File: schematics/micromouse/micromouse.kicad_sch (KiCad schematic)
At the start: 63 parts, among them J1 TOF_LEFT, J10 MotorB_Conn, J11 BMI_ConnB, J12 BMI_ConnA, J13 StepDown_{In+}, J14 StepDown_{In-}, J15 StepDown_{Out+}, J16 StepDown_{Out-}, J2 TOF_FRONTLEFT, J3 TOF_FRONTRIGHT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

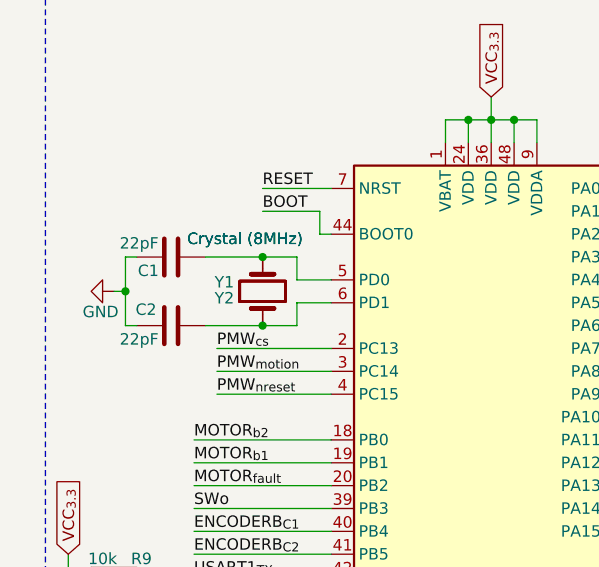
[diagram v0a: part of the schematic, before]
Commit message: Schematic/PCB: Add missing resistor for Crystal, based on STM's AN2586 (Getting started with STM32F10xxx hardware development).
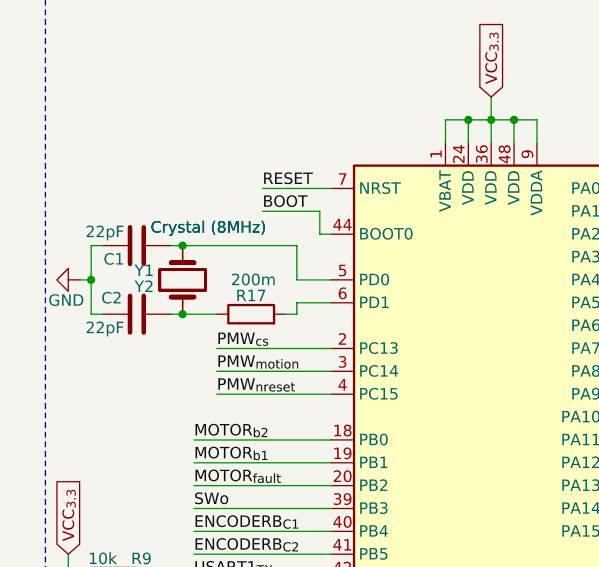
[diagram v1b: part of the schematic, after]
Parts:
- added R17: 200m, Resistor_SMD:R_0805_2012Metric_Pad1.20x1.40mm_HandSolder, symbol Device:R
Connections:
- net at C2.1, Y1.1, Y2.1: now also R17.1; no longer U1.6 (PD1)
- new net: R17.2, U1.6 (PD1)
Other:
- moved on the sheet: C1, C2, Y1, Y2
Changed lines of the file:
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@@
 	)
 	(junction
+		(at 27.94 43.18)
+		(diameter 0)
+		(color 0 0 0 0)
+	)
+	(junction
 		(at 60.96 111.76)
 		(diameter 0)
@@
 	)
 	(junction
-		(at 36.83 44.45)
-		(diameter 0)
-		(color 0 0 0 0)
-	)
-	(junction
 		(at 193.04 120.65)
 		(diameter 0)
@@
 	)
 	(junction
-		(at 36.83 52.07)
-		(diameter 0)
-		(color 0 0 0 0)
-	)
-	(junction
 		(at 123.19 135.89)
 		(diameter 0)
@@
 	)
 	(junction
-		(at 21.59 48.26)
+		(at 17.78 46.99)
 		(diameter 0)
 		(color 0 0 0 0)
@@
 	)
 	(junction
+		(at 27.94 50.8)
+		(diameter 0)
+		(color 0 0 0 0)
+	)
+	(junction
 		(at 255.27 123.19)
 		(diameter 0)
@@
 	(wire
 		(pts
-			(xy 30.48 52.07) (xy 36.83 52.07)
+			(xy 26.67 50.8) (xy 27.94 50.8)
 		)
 		(stroke
@@
 	(wire
 		(pts
-			(xy 40.64 52.07) (xy 36.83 52.07)
-		)
-		(stroke
-			(width 0)
-			(type default)
-		)
-	)
-	(wire
-		(pts
 			(xy 167.64 74.93) (xy 167.64 92.71)
 		)
@@
 	(wire
 		(pts
-			(xy 40.64 44.45) (xy 40.64 46.99)
+			(xy 40.64 43.18) (xy 40.64 46.99)
 		)
 		(stroke
@@
 	(wire
 		(pts
-			(xy 22.86 44.45) (xy 21.59 44.45)
+			(xy 19.05 43.18) (xy 17.78 43.18)
 		)
 		(stroke
@@
 	(wire
 		(pts
-			(xy 21.59 44.45) (xy 21.59 48.26)
+			(xy 17.78 43.18) (xy 17.78 46.99)
 		)
 		(stroke
@@
 	(wire
 		(pts
-			(xy 20.32 48.26) (xy 21.59 48.26)
+			(xy 16.51 46.99) (xy 17.78 46.99)
 		)
 		(stroke
@@
 	(wire
 		(pts
-			(xy 21.59 48.26) (xy 21.59 52.07)
+			(xy 17.78 46.99) (xy 17.78 50.8)
 		)
 		(stroke
@@
 	(wire
 		(pts
+			(xy 27.94 50.8) (xy 31.75 50.8)
+		)
+		(stroke
+			(width 0)
+			(type default)
+		)
+	)
+	(wire
+		(pts
 			(xy 130.81 187.96) (xy 138.43 187.96)
 		)
@@
 	(wire
 		(pts
+			(xy 27.94 43.18) (xy 40.64 43.18)
+		)
+		(stroke
+			(width 0)
+			(type default)
+		)
+	)
+	(wire
+		(pts
 			(xy 172.72 76.2) (xy 172.72 92.71)
 		)
@@
 	(wire
 		(pts
-			(xy 21.59 52.07) (xy 22.86 52.07)
+			(xy 17.78 50.8) (xy 19.05 50.8)
 		)
 		(stroke
@@
 	(wire
 		(pts
-			(xy 40.64 49.53) (xy 40.64 52.07)
-		)
-		(stroke
-			(width 0)
-			(type default)
-		)
-	)
-	(wire
-		(pts
-			(xy 36.83 44.45) (xy 40.64 44.45)
+			(xy 40.64 49.53) (xy 40.64 50.8)
 		)
 		(stroke
@@
 	(wire
 		(pts
-			(xy 30.48 44.45) (xy 36.83 44.45)
+			(xy 26.67 43.18) (xy 27.94 43.18)
 		)
 		(stroke
@@
 		)
 	)
+	(wire
+		(pts
+			(xy 39.37 50.8) (xy 40.64 50.8)
+		)
+		(stroke
+			(width 0)
+			(type default)
+		)
+	)
 	(rectangle
 		(start 12.7 12.7)
@@
 	(symbol
 		(lib_id "power:GND")
-		(at 20.32 48.26 270)
+		(at 16.51 46.99 270)
 		(unit 1)
 		(exclude_from_sim no)
@@
 		(dnp no)
 		(property "Reference" "#PWR014"
-			(at 13.97 48.26 0)
+			(at 10.16 46.99 0)
 			(effects
 				(font
@@
 		)
 		(property "Value" "GND"
-			(at 20.828 50.546 90)
+			(at 17.018 49.276 90)
 			(effects
 				(font
@@
 		)
 		(property "Footprint" ""
-			(at 20.32 48.26 0)
+			(at 16.51 46.99 0)
 			(effects
 				(font
@@
 		)
 		(property "Datasheet" ""
-			(at 20.32 48.26 0)
+			(at 16.51 46.99 0)
 			(effects
 				(font
@@
 		)
 		(property "Description" "Power symbol creates a global label with name \"GND\" , ground"
-			(at 20.32 48.26 0)
+			(at 16.51 46.99 0)
 			(effects
 				(font
@@
 	(symbol
 		(lib_id "Device:C")
-		(at 26.67 52.07 270)
+		(at 22.86 50.8 270)
 		(unit 1)
 		(exclude_from_sim no)
@@
 		(dnp no)
 		(property "Reference" "C2"
-			(at 23.876 50.292 90)
+			(at 20.066 49.022 90)
 			(effects
 				(font
@@
 		)
 		(property "Value" "22pF"
-			(at 23.114 53.594 90)
+			(at 19.304 52.324 90)
 			(effects
 				(font
@@
 		)
 		(property "Footprint" "Capacitor_SMD:C_0805_2012Metric_Pad1.18x1.45mm_HandSolder"
-			(at 22.86 53.0352 0)
+			(at 19.05 51.7652 0)
 			(effects
 				(font
@@
 		)
 		(property "Datasheet" "~"
-			(at 26.67 52.07 0)
+			(at 22.86 50.8 0)
 			(effects
 				(font
@@
 		)
 		(property "Description" "Unpolarized capacitor"
-			(at 26.67 52.07 0)
+			(at 22.86 50.8 0)
 			(effects
 				(font
@@
 	(symbol
 		(lib_id "Device:C")
-		(at 26.67 44.45 90)
+		(at 22.86 43.18 90)
 		(unit 1)
 		(exclude_from_sim no)
@@
 		(dnp no)
 		(property "Reference" "C1"
-			(at 24.13 45.974 90)
+			(at 20.32 44.704 90)
 			(effects
 				(font
@@
 		)
 		(property "Value" "22pF"
-			(at 23.114 42.926 90)
+			(at 19.304 41.656 90)
 			(effects
 				(font
@@
 		)
 		(property "Footprint" "Capacitor_SMD:C_0805_2012Metric_Pad1.18x1.45mm_HandSolder"
-			(at 30.48 43.4848 0)
+			(at 26.67 42.2148 0)
 			(effects
 				(font
@@
 		)
 		(property "Datasheet" "~"
-			(at 26.67 44.45 0)
+			(at 22.86 43.18 0)
 			(effects
 				(font
@@
 		)
 		(property "Description" "Unpolarized capacitor"
-			(at 26.67 44.45 0)
+			(at 22.86 43.18 0)
 			(effects
 				(font
@@
 	(symbol
 		(lib_id "Device:Crystal")
-		(at 36.83 48.26 90)
+		(at 27.94 46.99 90)
 		(unit 1)
 		(exclude_from_sim no)
@@
 		(dnp no)
 		(property "Reference" "Y1"
-			(at 31.496 47.244 90)
+			(at 22.606 45.974 90)
 			(effects
 				(font
@@
 		)
 		(property "Value" "Crystal (8MHz)"
-			(at 28.448 42.418 90)
+			(at 24.384 41.148 90)
 			(effects
 				(font
@@
 		)
 		(property "Footprint" "Crystal:Crystal_SMD_HC49-SD"
-			(at 36.83 48.26 0)
+			(at 27.94 46.99 0)
 			(effects
 				(font
@@
 		)
 		(property "Datasheet" "~"
-			(at 36.83 48.26 0)
+			(at 27.94 46.99 0)
 			(effects
 				(font
@@
 		)
 		(property "Description" "Two pin crystal"
-			(at 36.83 48.26 0)
+			(at 27.94 46.99 0)
 			(effects
 				(font
@@
 	(symbol
 		(lib_id "Device:Crystal")
-		(at 36.83 48.26 90)
+		(at 27.94 46.99 90)
 		(unit 1)
 		(exclude_from_sim no)
@@
 		(dnp no)
 		(property "Reference" "Y2"
-			(at 31.496 49.022 90)
+			(at 22.606 47.752 90)
 			(effects
 				(font
@@
 		)
 		(property "Value" "Crystal (8MHz)"
-			(at 28.448 42.418 90)
+			(at 24.384 41.148 90)
 			(effects
 				(font
@@
 		)
 		(property "Footprint" "Crystal:Crystal_HC49-4H_Vertical"
-			(at 36.83 48.26 0)
+			(at 27.94 46.99 0)
 			(effects
 				(font
@@
 		)
 		(property "Datasheet" "~"
-			(at 36.83 48.26 0)
+			(at 27.94 46.99 0)
 			(effects
 				(font
@@
 		)
 		(property "Description" "Two pin crystal"
-			(at 36.83 48.26 0)
+			(at 27.94 46.99 0)
 			(effects
 				(font
@@
 					(unit 1)
 				)
+			)
+		)
+	)
+	(symbol
+		(lib_id "Device:R")
+		(at 35.56 50.8 90)
+		(unit 1)
+		(exclude_from_sim no)
+		(in_bom yes)
+		(on_board yes)
+		(dnp no)
+		(property "Reference" "R17"
+			(at 35.56 48.768 90)
+			(effects
+				(font
+					(size 1.27 1.27)
+				)
+			)
+		)
+		(property "Value" "200m"
+			(at 35.814 46.99 90)
+			(effects
+				(font
+					(size 1.27 1.27)
+				)
+			)
+		)
+		(property "Footprint" "Resistor_SMD:R_0805_2012Metric_Pad1.20x1.40mm_HandSolder"
+			(at 35.56 52.578 90)
+			(effects
+				(font
+					(size 1.27 1.27)
+				)
+				(hide yes)
+			)
+		)
+		(property "Datasheet" "~"
+			(at 35.56 50.8 0)
+			(effects
+				(font
+					(size 1.27 1.27)
+				)
+				(hide yes)
+			)
+		)
+		(property "Description" "Resistor"
+			(at 35.56 50.8 0)
+			(effects
+				(font
+					(size 1.27 1.27)
+				)
+				(hide yes)
+			)
+		)
+		(pin "2"
+		)
+		(pin "1"
+		)
+		(instances
+			(project "micromouse"
+				(path "/48923552-97ee-4377-b66c-70fa2ca23716"
+					(reference "R17")
+					(unit 1)
+				)

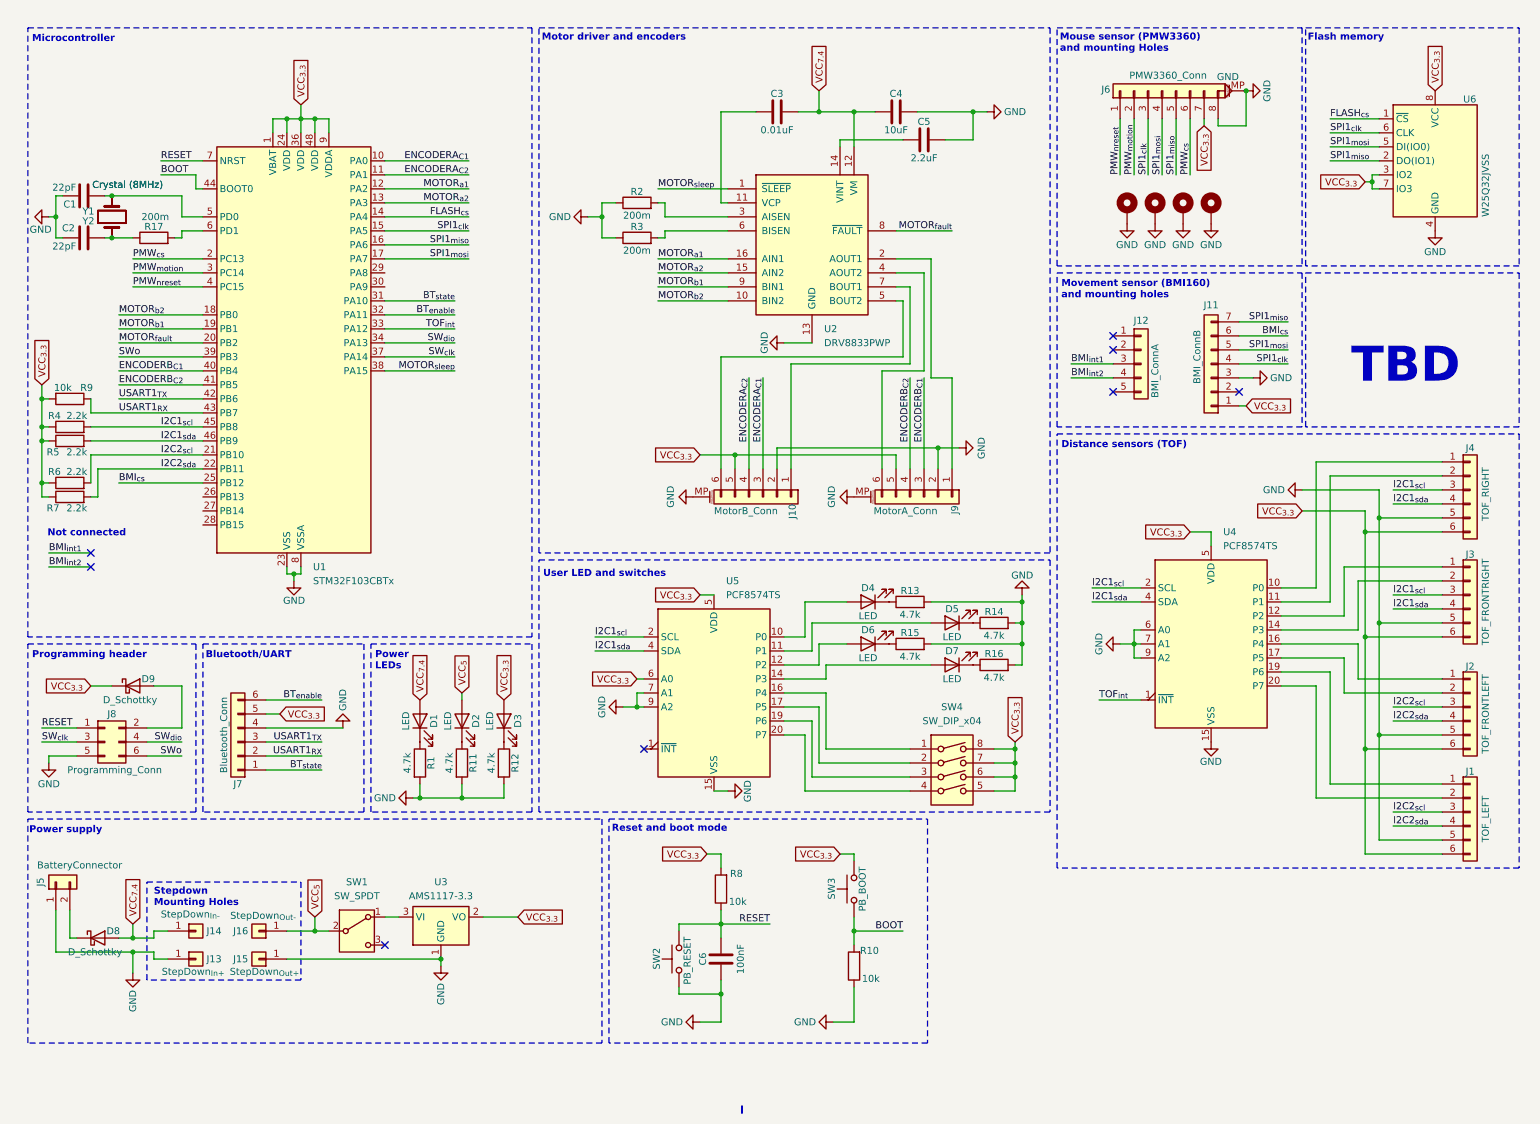
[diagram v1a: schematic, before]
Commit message: Schematic: * Add microSD card socket
PCB:
* Change BOOT and RESET buttons
* Add and connect microSD card socket
* Fix some CRC errors
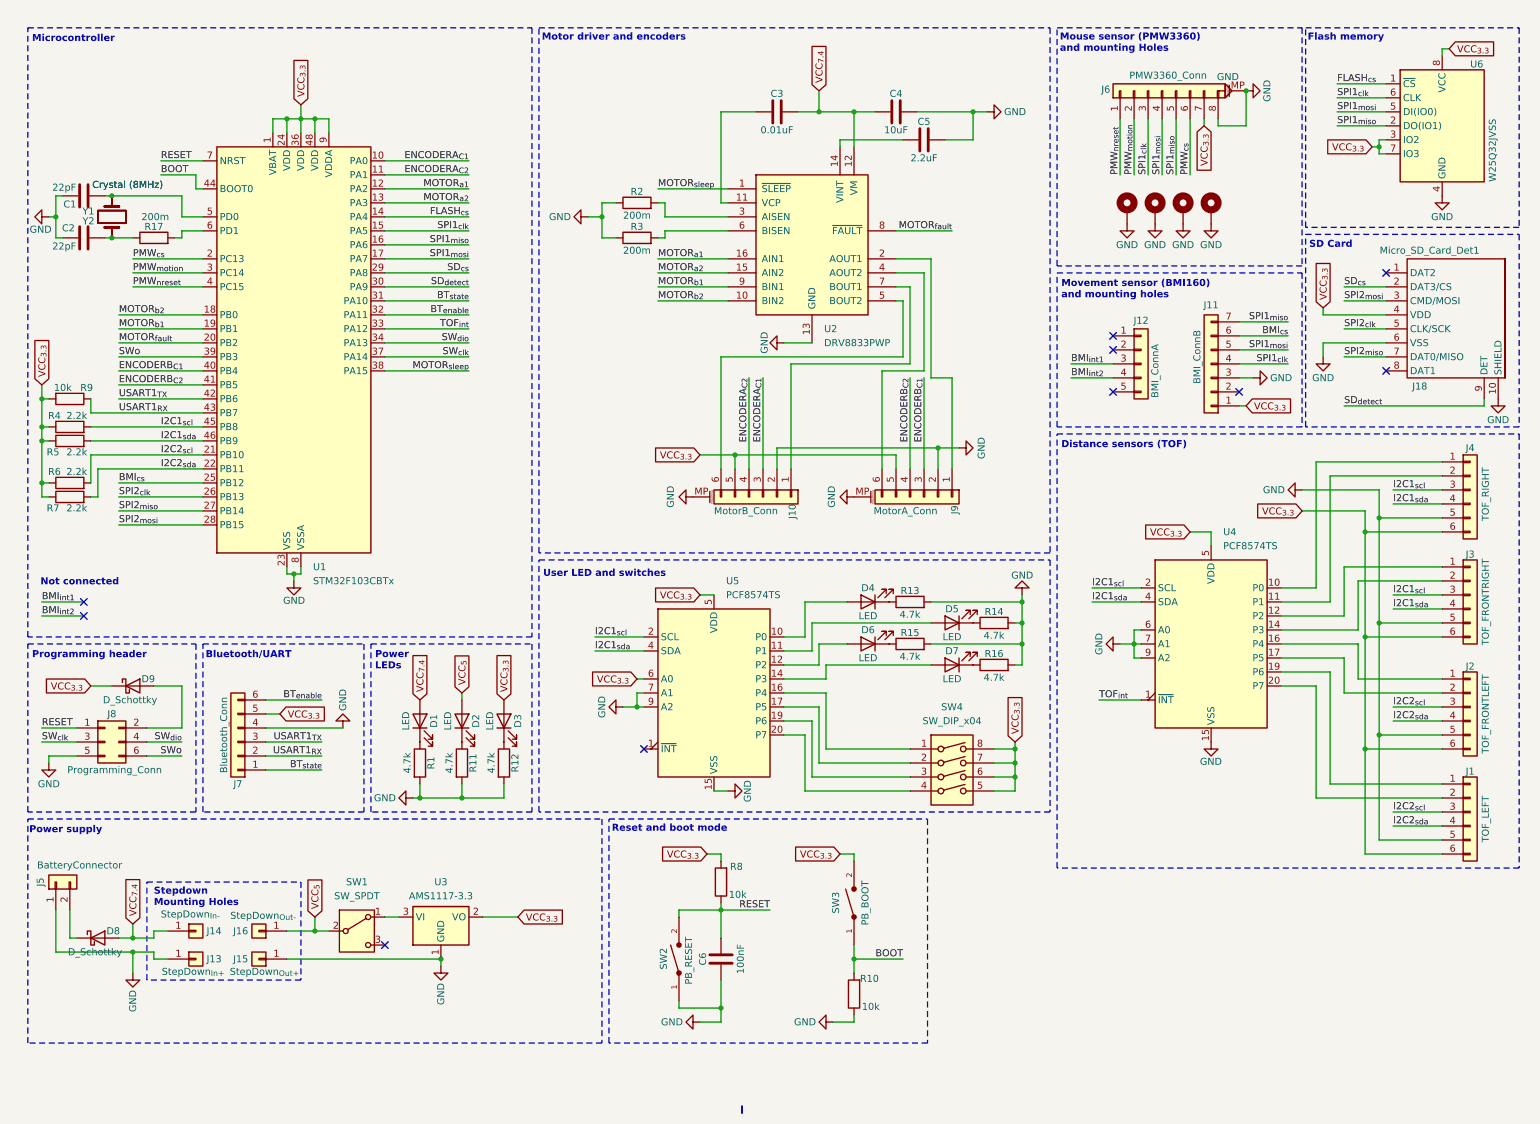
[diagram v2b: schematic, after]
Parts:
- added J18: Micro_SD_Card_Det1, Connector_Card:microSD_HC_Hirose_DM3D-SF, symbol Connector:Micro_SD_Card_Det1
- SW1: footprint Button_Switch_THT:SW_Slide_SPDT_Straight_CK_OS102011MS2Q -> Button_Switch_SMD:SW_SPDT_PCM12
- SW2, SW3: footprint Button_Switch_THT:SW_PUSH_6mm_H5mm -> FSMSM:TE_FSMSM; symbol Switch:SW_Push -> FSMSM:FSMSM; Availability (none) -> In Stock; Check_prices (none) -> https://www.snapeda.com/parts/FSMSM/TE+Connectivity+%252F+D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; Comment (none) -> 1437566-3; Configuration_Pole-Throw (none) -> Single Pole - Single Throw; Contact_Current_Rating (none) -> 50 mA; Description_1 (none) -> Tactile Switch; 50 mA; 12 VDC; 3.5 x 6 mm; SPST; Stainless;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; MANUFACTURER (none) -> TE Connectivity; MF (none) -> TE Connectivity; MP (none) -> FSMSM; PARTREV (none) -> C2; Package (none) -> None; Price (none) -> None; STANDARD (none) -> Manufacturer Recommendation; SnapEDA_Link (none) -> https://www.snapeda.com/parts/FSMSM/TE+Connectivity+%252F+D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
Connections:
- net GND: now also J18.10 (SHIELD), J18.6 (VSS)
- net VCC_{3.3}: now also J18.4 (VDD)
- net SPI2_{clk}: now reaches U1.26 (PB13)
- net SPI2_{clk}: now also J18.5 (CLK/SCK)
- net SPI2_{miso}: now reaches U1.27 (PB14)
- net SPI2_{miso}: now also J18.7 (DAT0/MISO)
- net SPI2_{mosi}: now reaches U1.28 (PB15)
- net SPI2_{mosi}: now also J18.3 (CMD/MOSI)
- net SD_{cs}: now reaches U1.29 (PA8)
- net SD_{cs}: now also J18.2 (DAT3/CS)
- net SD_{detect}: now reaches U1.30 (PA9)
- net SD_{detect}: now also J18.9 (DET)
- no-connect marks 8 -> 10
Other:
- note added: "SD Card"
- note removed: "TBD"
- moved on the sheet: R10, R8, U6
